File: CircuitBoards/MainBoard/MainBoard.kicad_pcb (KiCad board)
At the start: 2 copper layers, 203.2 x 170.2 mm, 6 parts

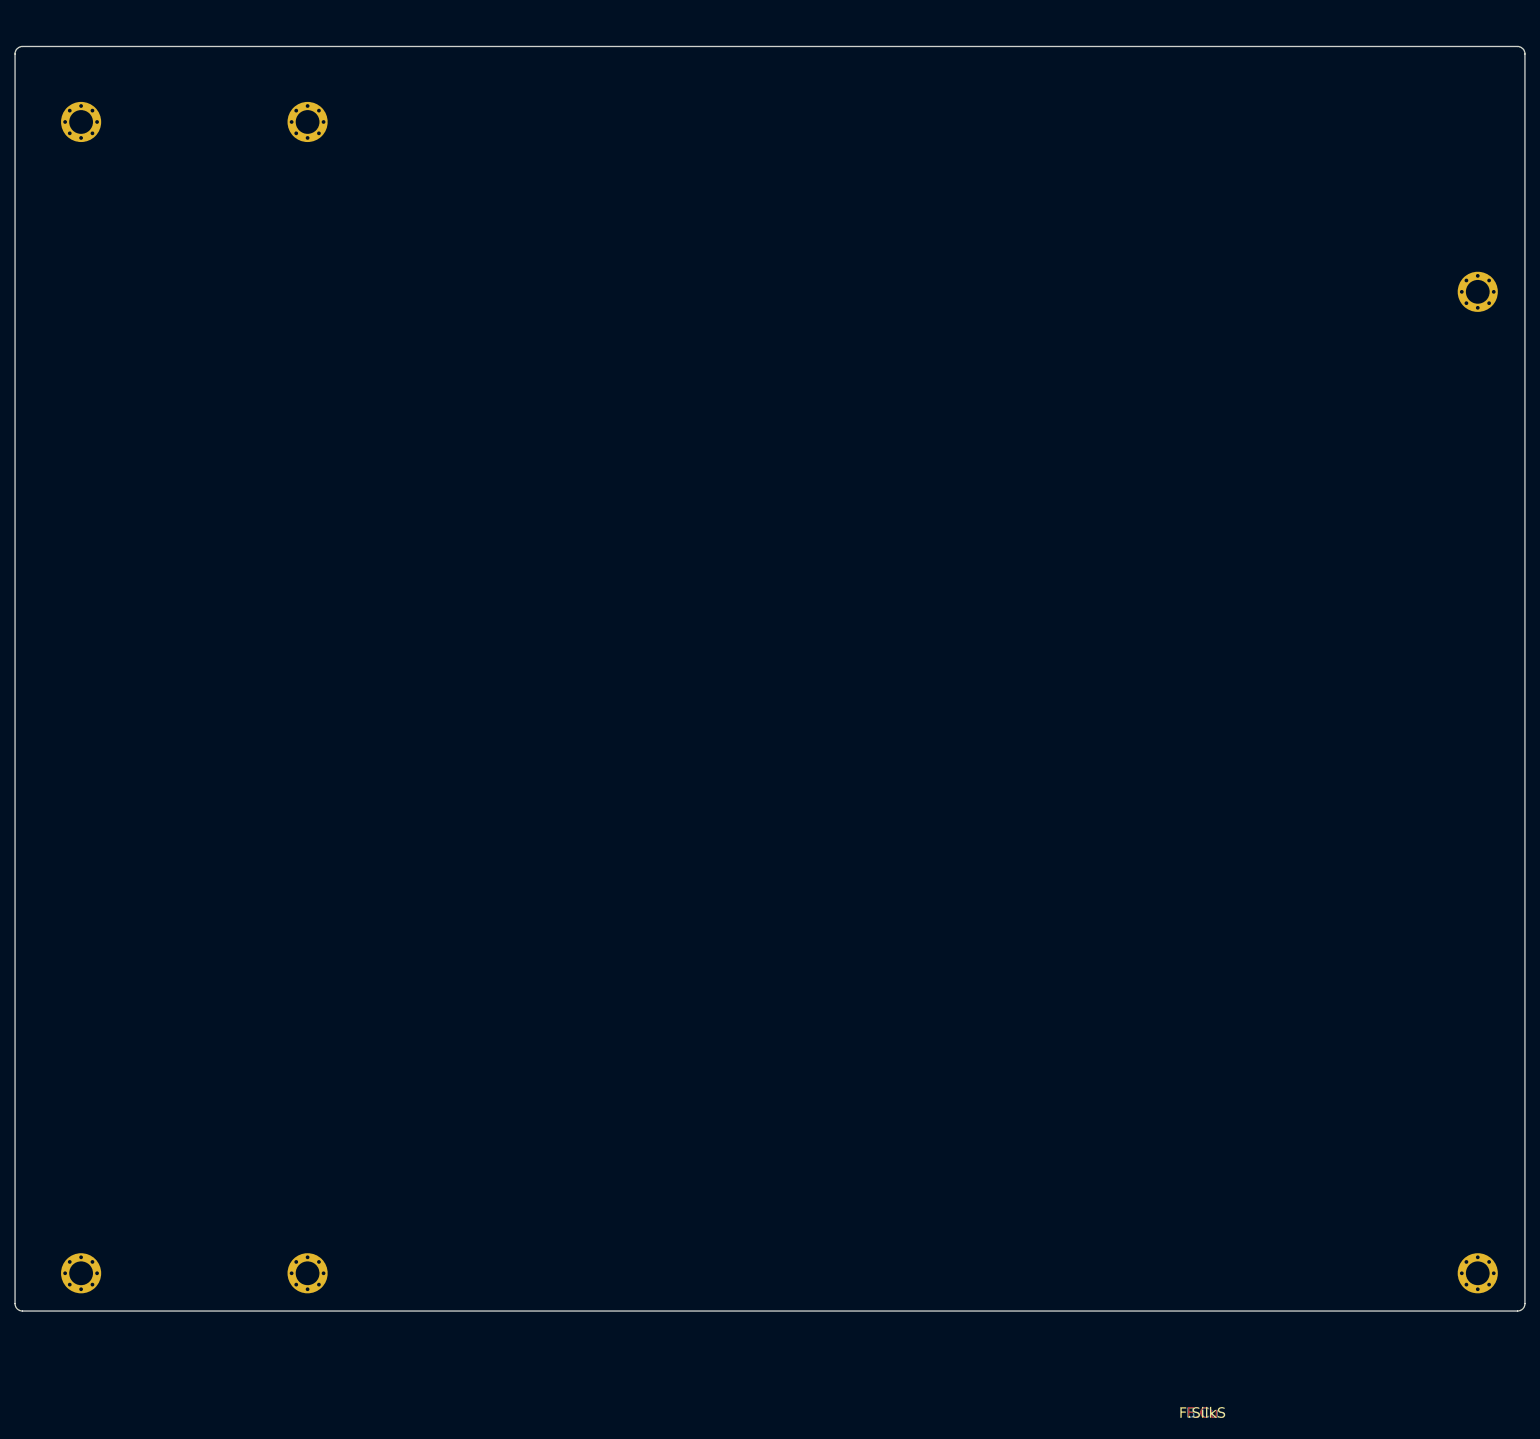
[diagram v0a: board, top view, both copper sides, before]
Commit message: MainBoard: Addition of the expansion slots
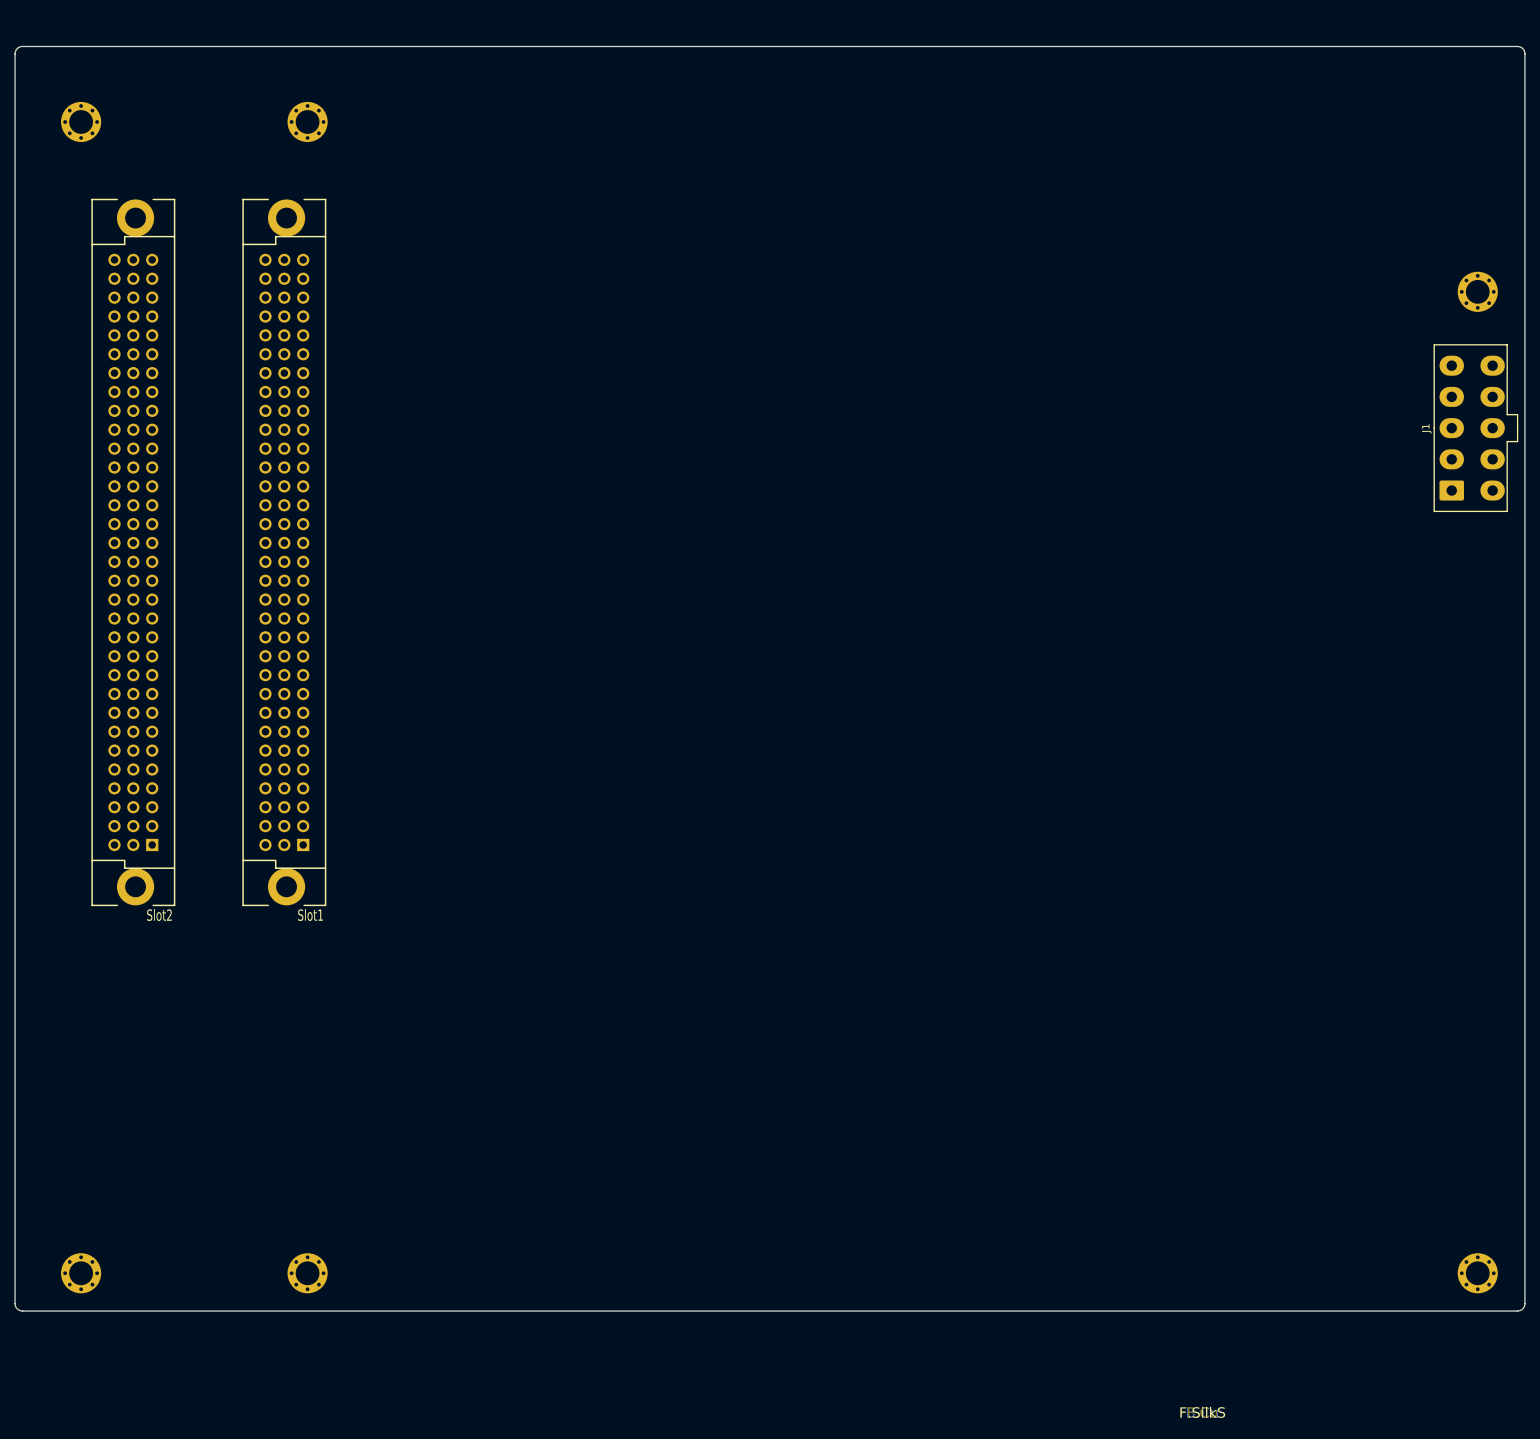
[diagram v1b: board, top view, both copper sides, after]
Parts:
- added J1: 39-28-1103, My68k:39-28-1103, F.Cu at (240.2, 74.7)
- added Slot1: DIN41612-C-96-F, My68k:DIN41612-C-96-F, F.Cu at (85.7, 122.4)
- added Slot2: DIN41612-C-96-F, My68k:DIN41612-C-96-F, F.Cu at (65.4, 122.4)

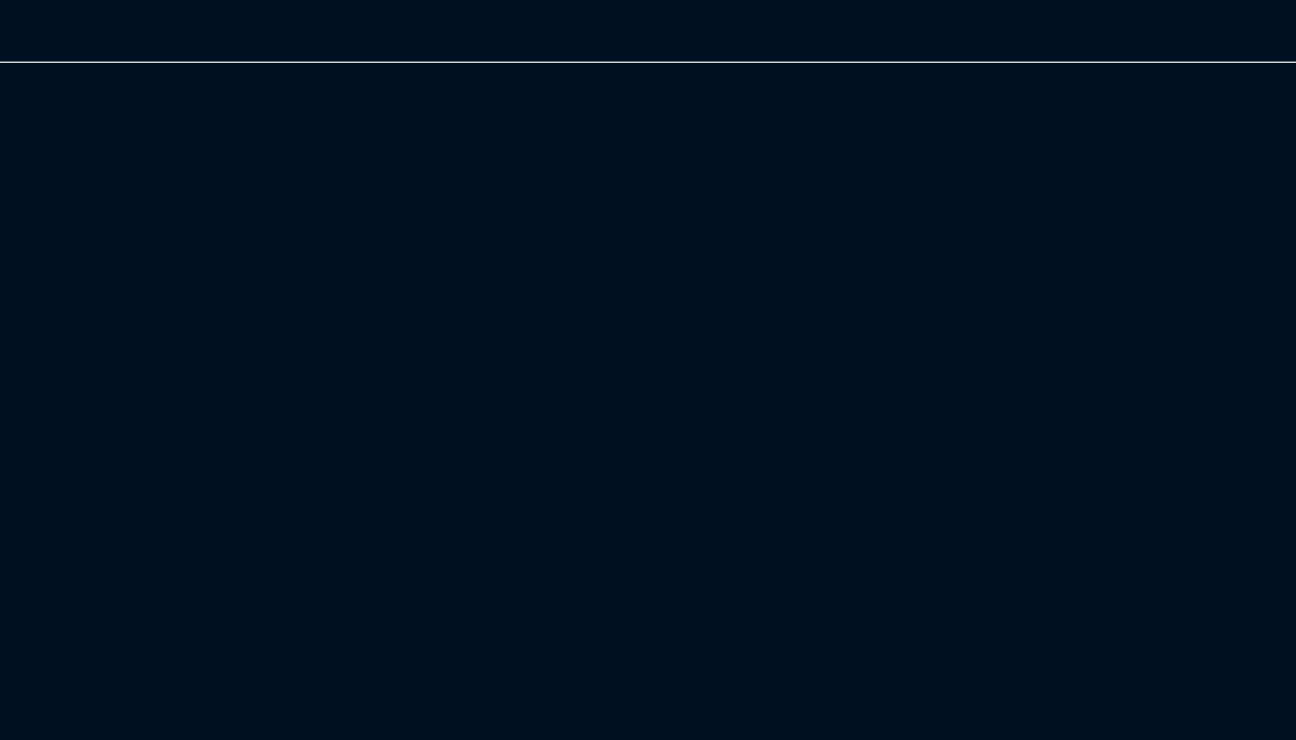
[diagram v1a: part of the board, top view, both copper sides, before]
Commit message: MainBoard: Addition of the DUART schematic
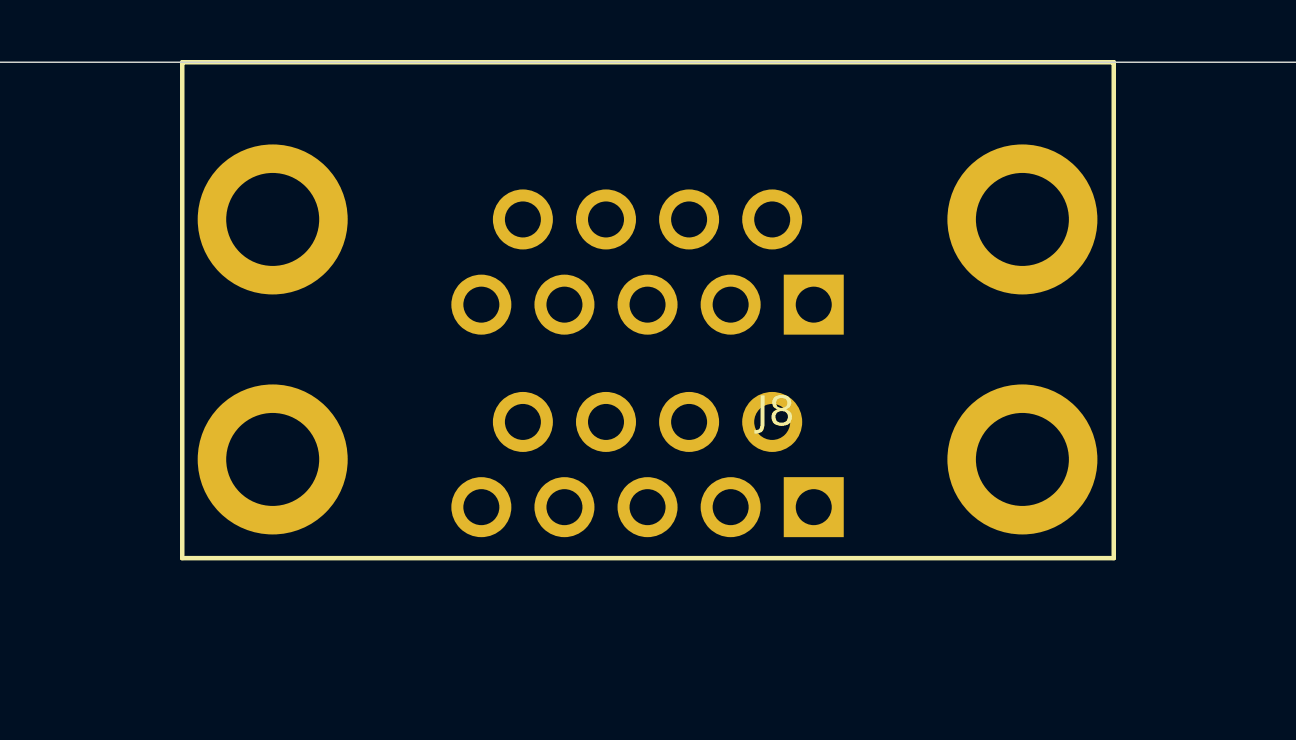
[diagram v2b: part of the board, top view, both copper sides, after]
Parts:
- added J8: 178-009-613, My68k:178-009-613, F.Cu at (204.7, 23.0)
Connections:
- Slot1 pad A20: (no net) -> /Expansion Slot 1/nBGIN
- Slot1 pad A21: (no net) -> /Expansion Slot 2/nBGIN
- Slot1 pad B20: (no net) -> /Expansion Slot 1/nIACKIN
- Slot1 pad B21: (no net) -> /Expansion Slot 2/nIACKIN
- Slot1 pad C21: (no net) -> /Expansion Slot 1/nID
- Slot2 pad A20: (no net) -> /Expansion Slot 2/nBGIN
- Slot2 pad B20: (no net) -> /Expansion Slot 2/nIACKIN
- Slot2 pad C21: (no net) -> /Expansion Slot 2/nID

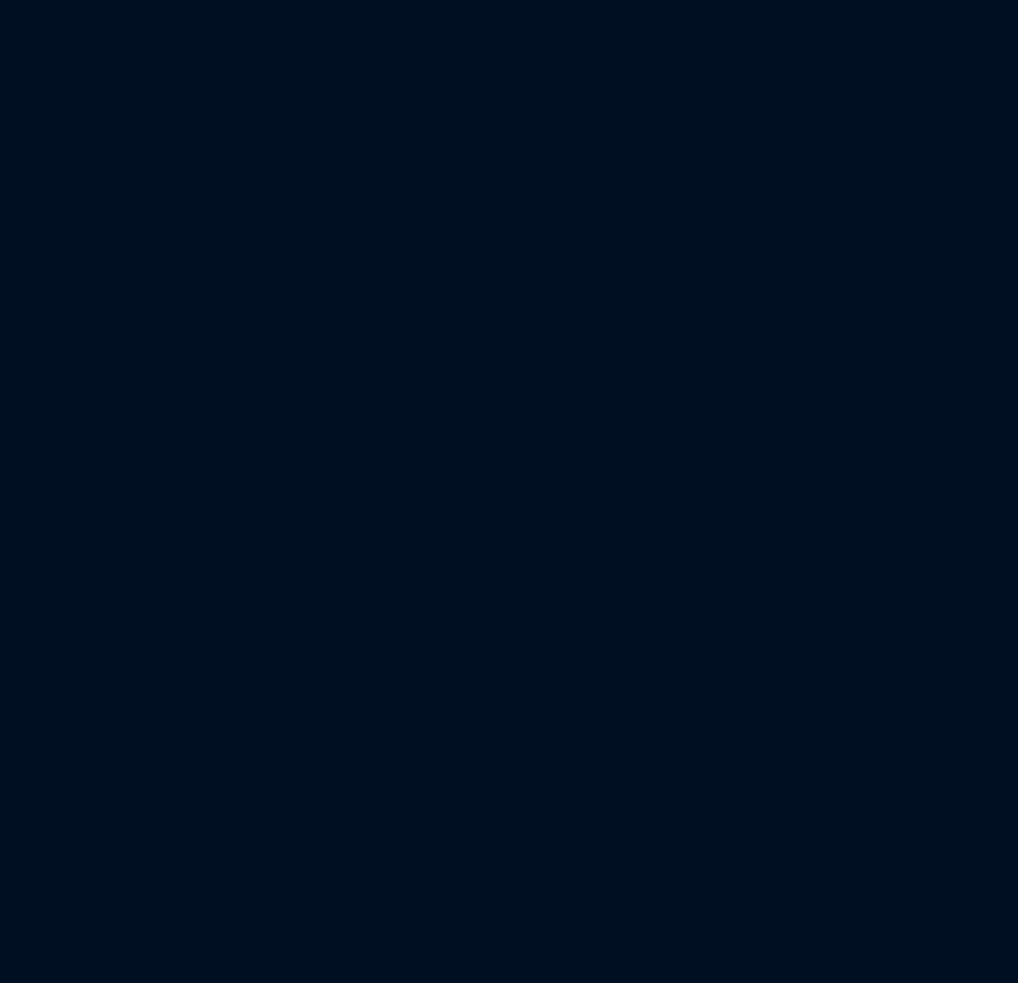
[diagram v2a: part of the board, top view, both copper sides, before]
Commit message: MainBoard: Addition of the ATA schematic
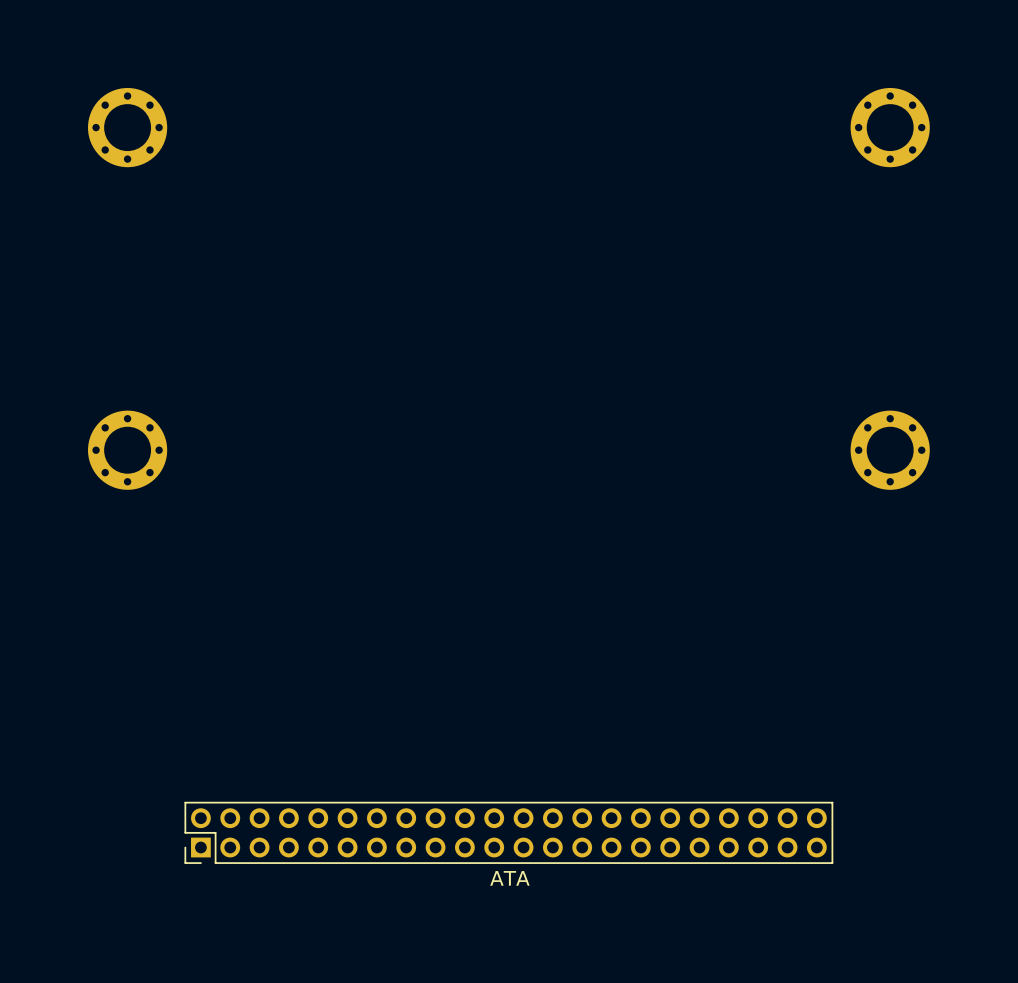
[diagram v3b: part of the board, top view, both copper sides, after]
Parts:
- added J29: ATA, My68k:87758-4416, F.Cu at (109.7, 75.0)
- added MH10: Mounting_Hole_M3, My68k:Mounting_Hole_M3, F.Cu at (156.7, 47.9)
- added MH7: Mounting_Hole_M3, My68k:Mounting_Hole_M3, F.Cu at (104.7, 25.9)
- added MH8: Mounting_Hole_M3, My68k:Mounting_Hole_M3, F.Cu at (156.7, 25.9)
- added MH9: Mounting_Hole_M3, My68k:Mounting_Hole_M3, F.Cu at (104.7, 47.9)

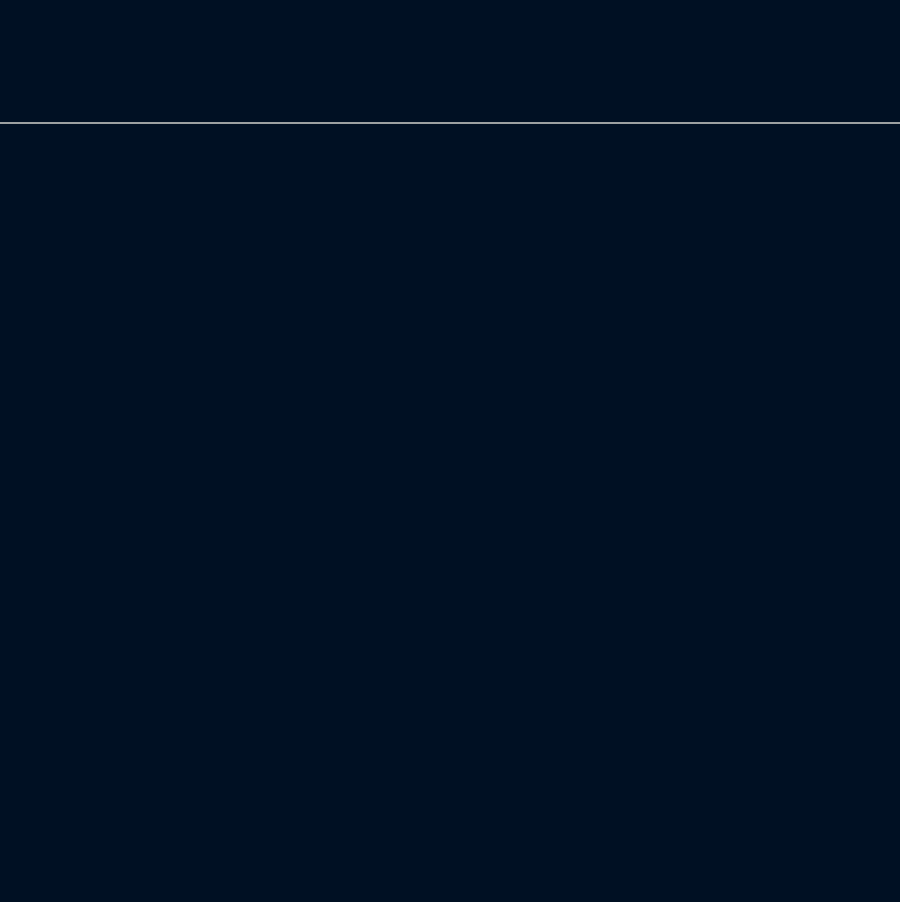
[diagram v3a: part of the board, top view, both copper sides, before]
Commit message: MainBoard: Addition of the PS2 schematic
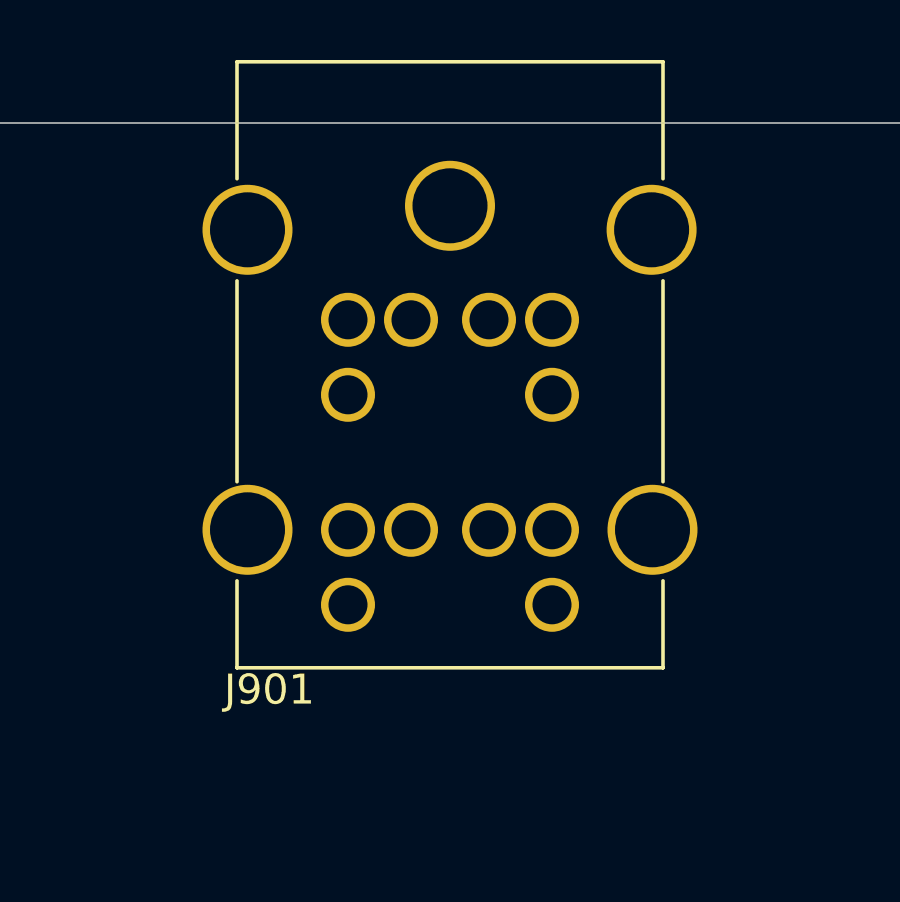
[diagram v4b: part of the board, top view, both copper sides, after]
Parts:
- added J901: DualMiniDin6, My68k:KMDGX-6S-6S-S4N, F.Cu at (230.4, 24.0)
